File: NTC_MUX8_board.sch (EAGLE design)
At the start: 64 parts, among them IC1 NINA-B306-00B-00, IC2 INA126E, IC3 MCP6001T_SOT23, IC4 MAX8559ETAAA+T, J1 USB4105-GF-A, J2 1761681-7, J3 DM3CS-SF-PEJMS, J4 DNP, J7 52808-2071, U1 TMUX1208PWR, U2 TMUX1208PWR, U3 TMUX1208PWR, U4 TMUX1208PWR, X1 22-23-2021

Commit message: beta finalizada
circuito listo a mi parecer
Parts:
- added C6, C7: 100nF, rcl:C-EUC0603
- C10, C3: value 2.2uF -> 100nF
- C11, C4: value 2.2uF -> 10uF
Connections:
- net 3V3_1: now also C6.1, C7.1
- net GND: now also C6.2, C7.2
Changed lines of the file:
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@@
 <part name="SUPPLY2" library="SparkFun-PowerSymbols" library_urn="urn:adsk.eagle:library:530" deviceset="V_USB" device=""/>
 <part name="GND5" library="audio amplifier example" library_urn="urn:adsk.eagle:library:970892" deviceset="GND" device="" value="SUP"/>
-<part name="L1" library="OPL_Ferrite_and_Magnetic_Bead" library_urn="urn:adsk.eagle:library:8004552" deviceset="SMD-FERRITE-BEAD-2500R-50MA(0603)" device="" package3d_urn="urn:adsk.eagle:package:8004622/1" value="2500R-50MA"/>
+<part name="L1" library="OPL_Ferrite_and_Magnetic_Bead" library_urn="urn:adsk.eagle:library:8004552" deviceset="SMD-FERRITE-BEAD-2500R-50MA(0603)" device="" package3d_urn="urn:adsk.eagle:package:8004622/1" override_package3d_urn="urn:adsk.eagle:package:39374540/2" override_package_urn="urn:adsk.eagle:footprint:8004597/1" value="2500R-50MA"/>
 <part name="GND6" library="audio amplifier example" library_urn="urn:adsk.eagle:library:970892" deviceset="GND" device="" value="SUP"/>
 <part name="GND7" library="audio amplifier example" library_urn="urn:adsk.eagle:library:970892" deviceset="GND" device="" value="SUP"/>
@@
 <part name="R4" library="rcl" library_urn="urn:adsk.eagle:library:334" deviceset="R-EU_" device="R0603" package3d_urn="urn:adsk.eagle:package:23555/3" value="1k"/>
 <part name="SUPPLY5" library="SparkFun-PowerSymbols" library_urn="urn:adsk.eagle:library:530" deviceset="V_USB" device=""/>
-<part name="C3" library="rcl" library_urn="urn:adsk.eagle:library:334" deviceset="C-EU" device="C0603" package3d_urn="urn:adsk.eagle:package:23616/2" value="2.2uF"/>
-<part name="C4" library="rcl" library_urn="urn:adsk.eagle:library:334" deviceset="C-EU" device="C0603" package3d_urn="urn:adsk.eagle:package:23616/2" value="2.2uF"/>
+<part name="C3" library="rcl" library_urn="urn:adsk.eagle:library:334" deviceset="C-EU" device="C0603" package3d_urn="urn:adsk.eagle:package:23616/2" value="100nF"/>
+<part name="C4" library="rcl" library_urn="urn:adsk.eagle:library:334" deviceset="C-EU" device="C0603" package3d_urn="urn:adsk.eagle:package:23616/2" value="10uF"/>
 <part name="SUPPLY24" library="Power_Symbols" library_urn="urn:adsk.eagle:library:16502351" deviceset="GND-BAR" device="" value="GND"/>
 <part name="GND10" library="audio amplifier example" library_urn="urn:adsk.eagle:library:970892" deviceset="GND" device="" value="SUP"/>
 <part name="C5" library="rcl" library_urn="urn:adsk.eagle:library:334" deviceset="C-EU" device="C0603" package3d_urn="urn:adsk.eagle:package:23616/2" value="0.01uF"/>
 <part name="GND11" library="audio amplifier example" library_urn="urn:adsk.eagle:library:970892" deviceset="GND" device="" value="SUP"/>
-<part name="C10" library="rcl" library_urn="urn:adsk.eagle:library:334" deviceset="C-EU" device="C0603" package3d_urn="urn:adsk.eagle:package:23616/2" value="2.2uF"/>
-<part name="C11" library="rcl" library_urn="urn:adsk.eagle:library:334" deviceset="C-EU" device="C0603" package3d_urn="urn:adsk.eagle:package:23616/2" value="2.2uF"/>
+<part name="C10" library="rcl" library_urn="urn:adsk.eagle:library:334" deviceset="C-EU" device="C0603" package3d_urn="urn:adsk.eagle:package:23616/2" value="100nF"/>
+<part name="C11" library="rcl" library_urn="urn:adsk.eagle:library:334" deviceset="C-EU" device="C0603" package3d_urn="urn:adsk.eagle:package:23616/2" value="10uF"/>
 <part name="GND12" library="audio amplifier example" library_urn="urn:adsk.eagle:library:970892" deviceset="GND" device="" value="SUP"/>
 <part name="U1" library="TMUX1208" deviceset="TMUX1208PWR" device="" override_package3d_urn="urn:adsk.eagle:package:39256706/3" override_package_urn="urn:adsk.eagle:footprint:39256707/1"/>
@@
 <part name="JP1" library="SparkFun-Jumpers" library_urn="urn:adsk.eagle:library:528" deviceset="JUMPER-SMT_3_NO" device="_NO-SILK" package3d_urn="urn:adsk.eagle:package:39284/1" override_package3d_urn="urn:adsk.eagle:package:39329052/2" override_package_urn="urn:adsk.eagle:footprint:39263/1"/>
 <part name="GND32" library="Arduino-supply" deviceset="GND" device="" value="GND"/>
-<part name="D2" library="SML-P12PTT86R" deviceset="SML-P12PTT86R" device="" override_package3d_urn="urn:adsk.eagle:package:39329460/2" override_package_urn="urn:adsk.eagle:footprint:39329461/1"/>
+<part name="D2" library="SML-P12PTT86R" deviceset="SML-P12PTT86R" device="" override_package3d_urn="urn:adsk.eagle:package:39374574/2" override_package_urn="urn:adsk.eagle:footprint:39374575/1"/>
 <part name="J6" library="con-lstb" library_urn="urn:adsk.eagle:library:162" deviceset="MA06-2" device="" package3d_urn="urn:adsk.eagle:package:8342/1" override_package3d_urn="urn:adsk.eagle:package:39329735/3" override_package_urn="urn:adsk.eagle:footprint:8289/1"/>
 <part name="J5" library="con-lstb" library_urn="urn:adsk.eagle:library:162" deviceset="MA04-2" device="" package3d_urn="urn:adsk.eagle:package:8368/1" override_package3d_urn="urn:adsk.eagle:package:39329712/4" override_package_urn="urn:adsk.eagle:footprint:8328/1"/>
@@
 <part name="R20" library="rcl" library_urn="urn:adsk.eagle:library:334" deviceset="R-EU_" device="R0603" package3d_urn="urn:adsk.eagle:package:23555/3" value="10k"/>
 <part name="R21" library="rcl" library_urn="urn:adsk.eagle:library:334" deviceset="R-EU_" device="R0603" package3d_urn="urn:adsk.eagle:package:23555/3" value="10k"/>
-<part name="R13" library="rcl" library_urn="urn:adsk.eagle:library:334" deviceset="R-EU_" device="R0603" package3d_urn="urn:adsk.eagle:package:23555/3" value="DNP"/>
-<part name="R14" library="rcl" library_urn="urn:adsk.eagle:library:334" deviceset="R-EU_" device="R0603" package3d_urn="urn:adsk.eagle:package:23555/3" value="DNP"/>
+<part name="R13" library="rcl" library_urn="urn:adsk.eagle:library:334" deviceset="R-EU_" device="R0603" package3d_urn="urn:adsk.eagle:package:23555/3" override_package3d_urn="urn:adsk.eagle:package:39374572/2" override_package_urn="urn:adsk.eagle:footprint:23044/1" value="DNP"/>
+<part name="R14" library="rcl" library_urn="urn:adsk.eagle:library:334" deviceset="R-EU_" device="R0603" package3d_urn="urn:adsk.eagle:package:23555/3" override_package3d_urn="urn:adsk.eagle:package:39374573/2" override_package_urn="urn:adsk.eagle:footprint:23044/1" value="DNP"/>
 <part name="SV1" library="con-lstb" library_urn="urn:adsk.eagle:library:162" deviceset="MA03-1" device="" package3d_urn="urn:adsk.eagle:package:8339/1" override_package3d_urn="urn:adsk.eagle:package:39362152/2" override_package_urn="urn:adsk.eagle:footprint:8281/1"/>
 <part name="X1" library="con-molex" library_urn="urn:adsk.eagle:library:165" deviceset="22-23-2021" device="" package3d_urn="urn:adsk.eagle:package:8078633/1" override_package3d_urn="urn:adsk.eagle:package:39362140/2" override_package_urn="urn:adsk.eagle:footprint:8078259/1"/>
 <part name="J7" library="52808-2071" deviceset="52808-2071" device="" override_package3d_urn="urn:adsk.eagle:package:39362400/2" override_package_urn="urn:adsk.eagle:footprint:39362401/1"/>
+<part name="C6" library="rcl" library_urn="urn:adsk.eagle:library:334" deviceset="C-EU" device="C0603" package3d_urn="urn:adsk.eagle:package:23616/2" override_package3d_urn="urn:adsk.eagle:package:39374531/2" override_package_urn="urn:adsk.eagle:footprint:23123/1" value="100nF"/>
+<part name="C7" library="rcl" library_urn="urn:adsk.eagle:library:334" deviceset="C-EU" device="C0603" package3d_urn="urn:adsk.eagle:package:23616/2" override_package3d_urn="urn:adsk.eagle:package:39374516/2" override_package_urn="urn:adsk.eagle:footprint:23123/1" value="100nF"/>
+<part name="GND9" library="audio amplifier example" library_urn="urn:adsk.eagle:library:970892" deviceset="GND" device="" value="SUP"/>
 </parts>
 <sheets>
@@
 <attribute name="VALUE" x="105.41" y="58.42" size="1.778" layer="96" align="center-left"/>
 </instance>
+<instance part="C6" gate="G$1" x="140.208" y="168.148" smashed="yes">
+<attribute name="NAME" x="141.732" y="168.529" size="1.778" layer="95"/>
+<attribute name="VALUE" x="141.732" y="163.449" size="1.778" layer="96"/>
+</instance>
+<instance part="C7" gate="G$1" x="150.368" y="168.148" smashed="yes">
+<attribute name="NAME" x="151.892" y="168.529" size="1.778" layer="95"/>
+<attribute name="VALUE" x="151.892" y="163.449" size="1.778" layer="96"/>
+</instance>
+<instance part="GND9" gate="G$1" x="145.288" y="160.528" smashed="yes"/>
 </instances>
 <busses>
@@
 <label x="157.48" y="132.08" size="1.016" layer="95" xref="yes"/>
 </segment>
+<segment>
+<pinref part="C6" gate="G$1" pin="2"/>
+<wire x1="140.208" y1="163.068" x2="140.208" y2="160.528" width="0.1524" layer="91"/>
+<wire x1="140.208" y1="160.528" x2="145.288" y2="160.528" width="0.1524" layer="91"/>
+<pinref part="C7" gate="G$1" pin="2"/>
+<wire x1="145.288" y1="160.528" x2="150.368" y2="160.528" width="0.1524" layer="91"/>
+<wire x1="150.368" y1="160.528" x2="150.368" y2="163.068" width="0.1524" layer="91"/>
+<pinref part="GND9" gate="G$1" pin="GND"/>
+<junction x="145.288" y="160.528"/>
+</segment>
 </net>
 <net name="N$1" class="0">
@@
 <pinref part="3V3T1" gate="G$1" pin="TP"/>
 </segment>
+<segment>
+<pinref part="C6" gate="G$1" pin="1"/>
+<wire x1="140.208" y1="170.688" x2="140.208" y2="172.72" width="0.1524" layer="91"/>
+<wire x1="140.208" y1="172.72" x2="144.78" y2="172.72" width="0.1524" layer="91"/>
+<pinref part="C7" gate="G$1" pin="1"/>
+<wire x1="144.78" y1="172.72" x2="150.368" y2="172.72" width="0.1524" layer="91"/>
+<wire x1="150.368" y1="172.72" x2="150.368" y2="170.688" width="0.1524" layer="91"/>
+<wire x1="144.78" y1="172.72" x2="144.78" y2="175.26" width="0.1524" layer="91"/>
+<junction x="144.78" y="172.72"/>
+<label x="144.78" y="175.26" size="1.016" layer="95" rot="R180" xref="yes"/>
+</segment>
 </net>

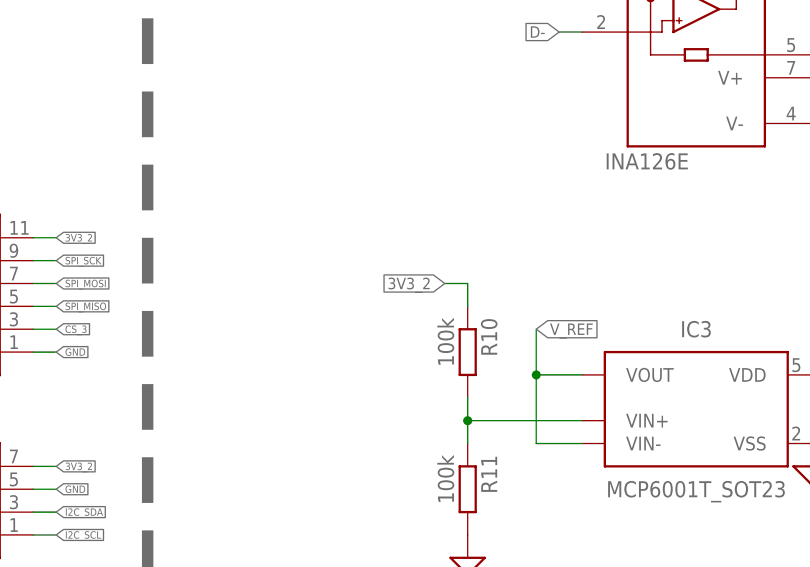
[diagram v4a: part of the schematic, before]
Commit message: minor corrections
corrección v en seguidor
y pistas
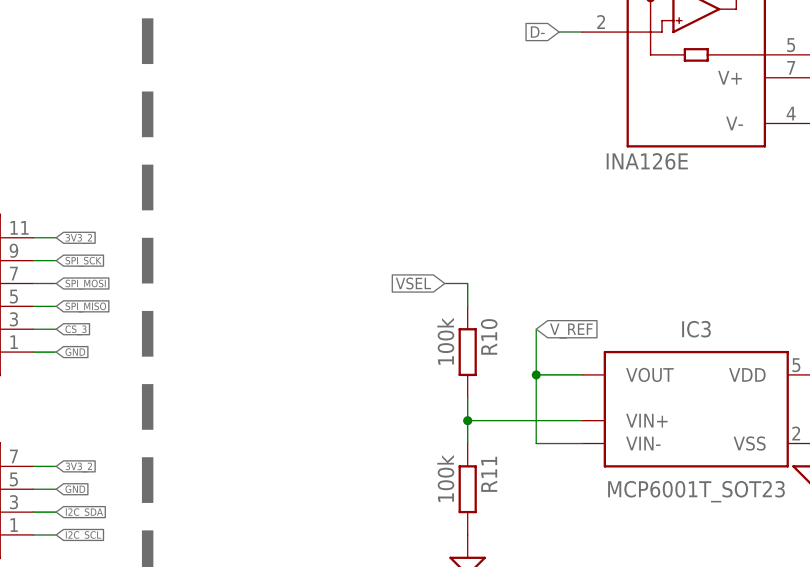
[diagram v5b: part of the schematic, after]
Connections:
- net 3V3_2: no longer R10.1
- net VSEL: now also R10.1
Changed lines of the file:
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@@
-</segment>
-<segment>
-<pinref part="R10" gate="G$1" pin="1"/>
-<wire x1="205.74" y1="40.64" x2="205.74" y2="43.18" width="0.1524" layer="91"/>
-<wire x1="205.74" y1="43.18" x2="203.2" y2="43.18" width="0.1524" layer="91"/>
-<label x="203.2" y="43.18" size="1.27" layer="95" rot="R180" xref="yes"/>
 </segment>
 <segment>
@@
 <label x="190.5" y="129.54" size="1.27" layer="95" xref="yes"/>
 </segment>
-</net>
+<segment>
+<pinref part="R10" gate="G$1" pin="1"/>
+<wire x1="205.74" y1="40.64" x2="205.74" y2="43.18" width="0.1524" layer="91"/>
+<wire x1="205.74" y1="43.18" x2="203.2" y2="43.18" width="0.1524" layer="91"/>
+<label x="203.2" y="43.18" size="1.27" layer="95" rot="R180" xref="yes"/>
+</segment>
+</net>

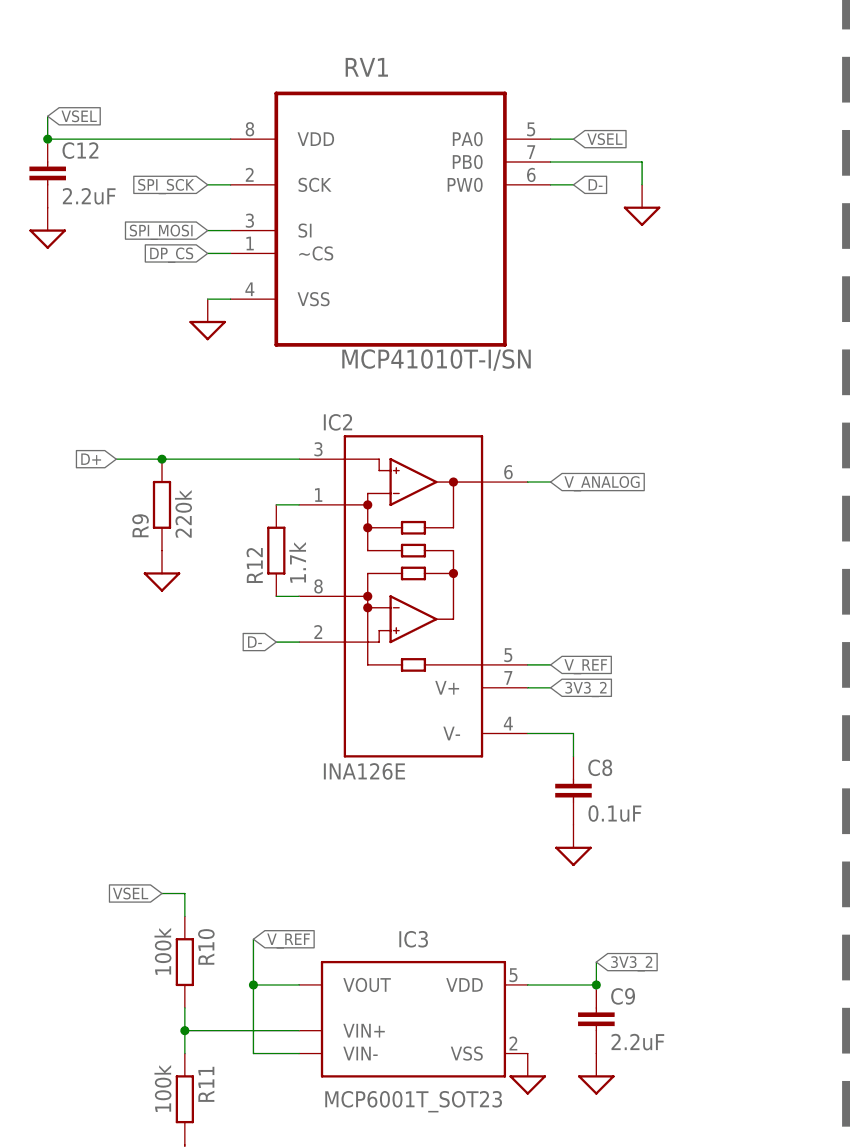
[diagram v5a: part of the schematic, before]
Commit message: test points on front end
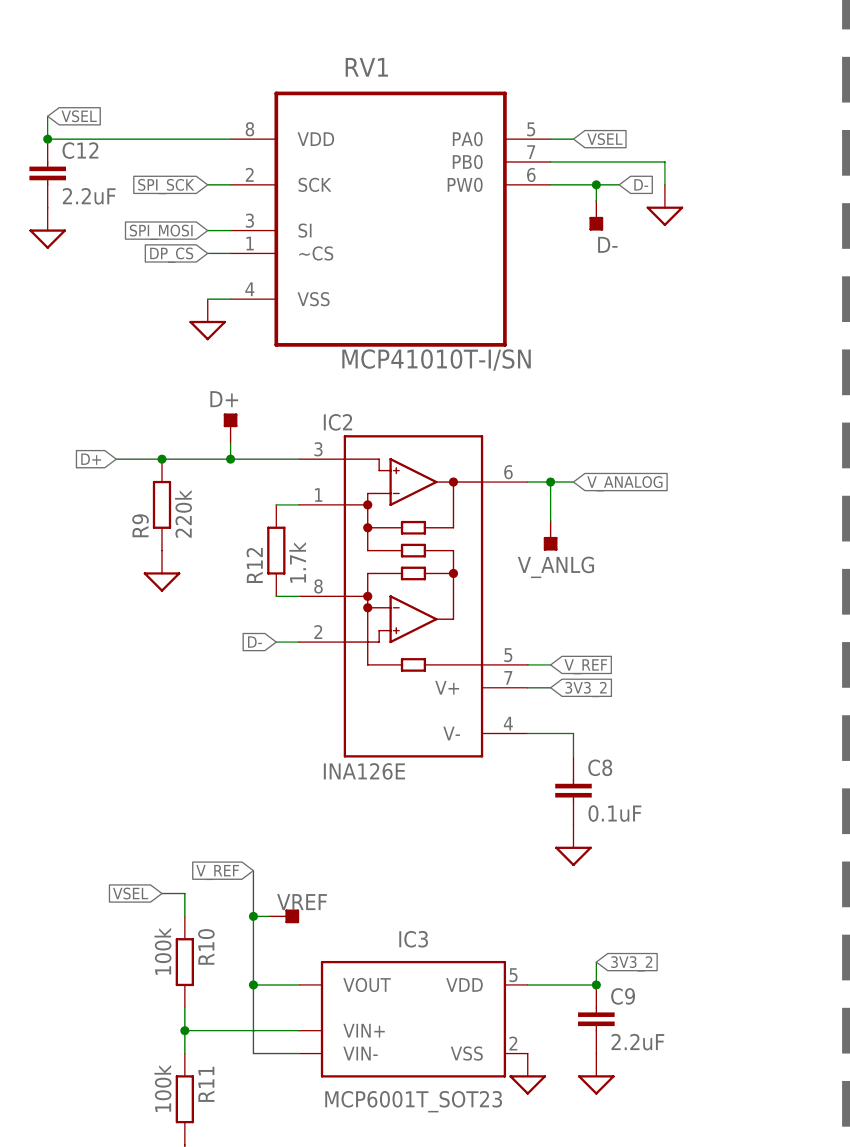
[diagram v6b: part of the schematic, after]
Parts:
- added D+, D-, VREF, V_ANLG: TESTPOINT_TPS-SMD-10SN, 52101-101-REV-A_v16:TESTPOINT_TPS-SMD-10SN
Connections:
- net D+: now also D+.TP
- net D-: now also D-.TP
- net V_ANALOG: now also V_ANLG.TP
- net V_REF: now also VREF.TP
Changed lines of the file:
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@@
 <part name="C7" library="rcl" library_urn="urn:adsk.eagle:library:334" deviceset="C-EU" device="C0603" package3d_urn="urn:adsk.eagle:package:23616/2" override_package3d_urn="urn:adsk.eagle:package:39374516/2" override_package_urn="urn:adsk.eagle:footprint:23123/1" value="100nF"/>
 <part name="GND9" library="audio amplifier example" library_urn="urn:adsk.eagle:library:970892" deviceset="GND" device="" value="SUP"/>
+<part name="V_ANLG" library="52101-101-REV-A_v16" library_urn="urn:adsk.eagle:library:21899384" deviceset="TESTPOINT_TPS" device="-SMD-10SN" package3d_urn="urn:adsk.eagle:package:15662280/2"/>
+<part name="D+" library="52101-101-REV-A_v16" library_urn="urn:adsk.eagle:library:21899384" deviceset="TESTPOINT_TPS" device="-SMD-10SN" package3d_urn="urn:adsk.eagle:package:15662280/2"/>
+<part name="VREF" library="52101-101-REV-A_v16" library_urn="urn:adsk.eagle:library:21899384" deviceset="TESTPOINT_TPS" device="-SMD-10SN" package3d_urn="urn:adsk.eagle:package:15662280/2"/>
+<part name="D-" library="52101-101-REV-A_v16" library_urn="urn:adsk.eagle:library:21899384" deviceset="TESTPOINT_TPS" device="-SMD-10SN" package3d_urn="urn:adsk.eagle:package:15662280/2"/>
 </parts>
 <sheets>
@@
 <attribute name="VALUE" x="222.97993125" y="101.525" size="2.08526875" layer="96" ratio="10" rot="SR0"/>
 </instance>
-<instance part="GND26" gate="G$1" x="256.54" y="121.92" smashed="yes"/>
+<instance part="GND26" gate="G$1" x="259.08" y="121.92" smashed="yes"/>
 <instance part="C12" gate="G$1" x="190.5" y="124.46" smashed="yes">
 <attribute name="NAME" x="192.024" y="124.841" size="1.778" layer="95"/>
@@
 </instance>
 <instance part="GND9" gate="G$1" x="145.288" y="160.528" smashed="yes"/>
+<instance part="V_ANLG" gate="G$1" x="246.38" y="82.042" smashed="yes" rot="R180">
+<attribute name="NAME" x="251.3838" y="80.5815" size="1.778" layer="95" rot="R180"/>
+</instance>
+<instance part="D+" gate="G$1" x="210.82" y="95.758" smashed="yes">
+<attribute name="NAME" x="208.3562" y="97.2185" size="1.778" layer="95"/>
+</instance>
+<instance part="VREF" gate="G$1" x="217.678" y="40.64" smashed="yes" rot="R270">
+<attribute name="NAME" x="215.9762" y="41.3385" size="1.778" layer="95"/>
+</instance>
+<instance part="D-" gate="G$1" x="251.46" y="117.602" smashed="yes" rot="R180">
+<attribute name="NAME" x="253.9238" y="116.1415" size="1.778" layer="95" rot="R180"/>
+</instance>
 </instances>
 <busses>
@@
 <segment>
 <pinref part="RV1" gate="A" pin="PB0"/>
-<wire x1="246.38" y1="124.46" x2="256.54" y2="124.46" width="0.1524" layer="91"/>
+<wire x1="246.38" y1="124.46" x2="259.08" y2="124.46" width="0.1524" layer="91"/>
 <pinref part="GND26" gate="G$1" pin="GND"/>
-<wire x1="256.54" y1="124.46" x2="256.54" y2="121.92" width="0.1524" layer="91"/>
+<wire x1="259.08" y1="124.46" x2="259.08" y2="121.92" width="0.1524" layer="91"/>
 </segment>
 <segment>
@@
 <segment>
 <pinref part="IC2" gate="G$1" pin="+IN"/>
-<wire x1="218.44" y1="91.44" x2="203.2" y2="91.44" width="0.1524" layer="91"/>
+<wire x1="218.44" y1="91.44" x2="210.82" y2="91.44" width="0.1524" layer="91"/>
 <pinref part="R9" gate="G$1" pin="2"/>
+<wire x1="210.82" y1="91.44" x2="203.2" y2="91.44" width="0.1524" layer="91"/>
 <wire x1="203.2" y1="91.44" x2="198.12" y2="91.44" width="0.1524" layer="91"/>
 <junction x="203.2" y="91.44"/>
 <label x="198.12" y="91.44" size="1.27" layer="95" rot="R180" xref="yes"/>
+<pinref part="D+" gate="G$1" pin="TP"/>
+<wire x1="210.82" y1="93.218" x2="210.82" y2="91.44" width="0.1524" layer="91"/>
+<junction x="210.82" y="91.44"/>
 </segment>
 </net>
@@
 <pinref part="IC2" gate="G$1" pin="OUT"/>
 <wire x1="243.84" y1="88.9" x2="246.38" y2="88.9" width="0.1524" layer="91"/>
-<label x="246.38" y="88.9" size="1.27" layer="95" xref="yes"/>
+<label x="248.92" y="88.9" size="1.27" layer="95" xref="yes"/>
+<pinref part="V_ANLG" gate="G$1" pin="TP"/>
+<wire x1="246.38" y1="88.9" x2="248.92" y2="88.9" width="0.1524" layer="91"/>
+<wire x1="246.38" y1="84.582" x2="246.38" y2="88.9" width="0.1524" layer="91"/>
+<junction x="246.38" y="88.9"/>
 </segment>
 <segment>
@@
 <pinref part="IC3" gate="G$1" pin="VOUT"/>
 <wire x1="213.36" y1="33.02" x2="218.44" y2="33.02" width="0.1524" layer="91"/>
-<wire x1="213.36" y1="33.02" x2="213.36" y2="38.1" width="0.1524" layer="91"/>
 <junction x="213.36" y="33.02"/>
-<label x="213.36" y="38.1" size="1.27" layer="95" xref="yes"/>
+<label x="213.36" y="45.72" size="1.27" layer="95" rot="R180" xref="yes"/>
+<wire x1="213.36" y1="33.02" x2="213.36" y2="40.64" width="0.1524" layer="91"/>
+<pinref part="VREF" gate="G$1" pin="TP"/>
+<wire x1="213.36" y1="40.64" x2="213.36" y2="45.72" width="0.1524" layer="91"/>
+<wire x1="215.138" y1="40.64" x2="213.36" y2="40.64" width="0.1524" layer="91"/>
+<junction x="213.36" y="40.64"/>
 </segment>
 </net>
@@
 <segment>
 <pinref part="RV1" gate="A" pin="PW0"/>
-<wire x1="246.38" y1="121.92" x2="248.92" y2="121.92" width="0.1524" layer="91"/>
-<label x="248.92" y="121.92" size="1.27" layer="95" xref="yes"/>
+<wire x1="246.38" y1="121.92" x2="251.46" y2="121.92" width="0.1524" layer="91"/>
+<label x="254" y="121.92" size="1.27" layer="95" xref="yes"/>
+<pinref part="D-" gate="G$1" pin="TP"/>
+<wire x1="251.46" y1="121.92" x2="254" y2="121.92" width="0.1524" layer="91"/>
+<wire x1="251.46" y1="120.142" x2="251.46" y2="121.92" width="0.1524" layer="91"/>
+<junction x="251.46" y="121.92"/>
 </segment>
 </net>
